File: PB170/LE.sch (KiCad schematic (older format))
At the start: 7 parts

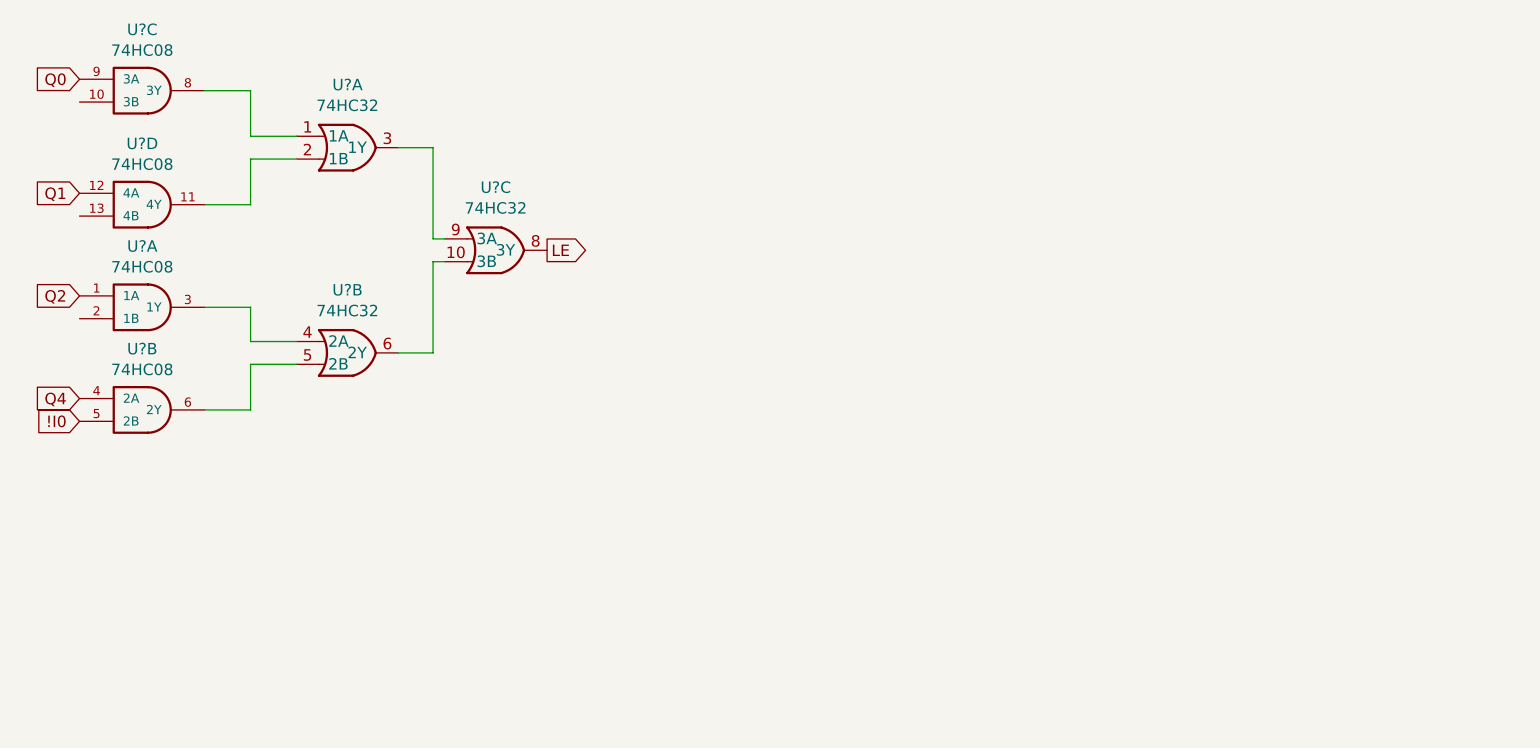
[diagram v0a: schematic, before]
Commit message: added some labels
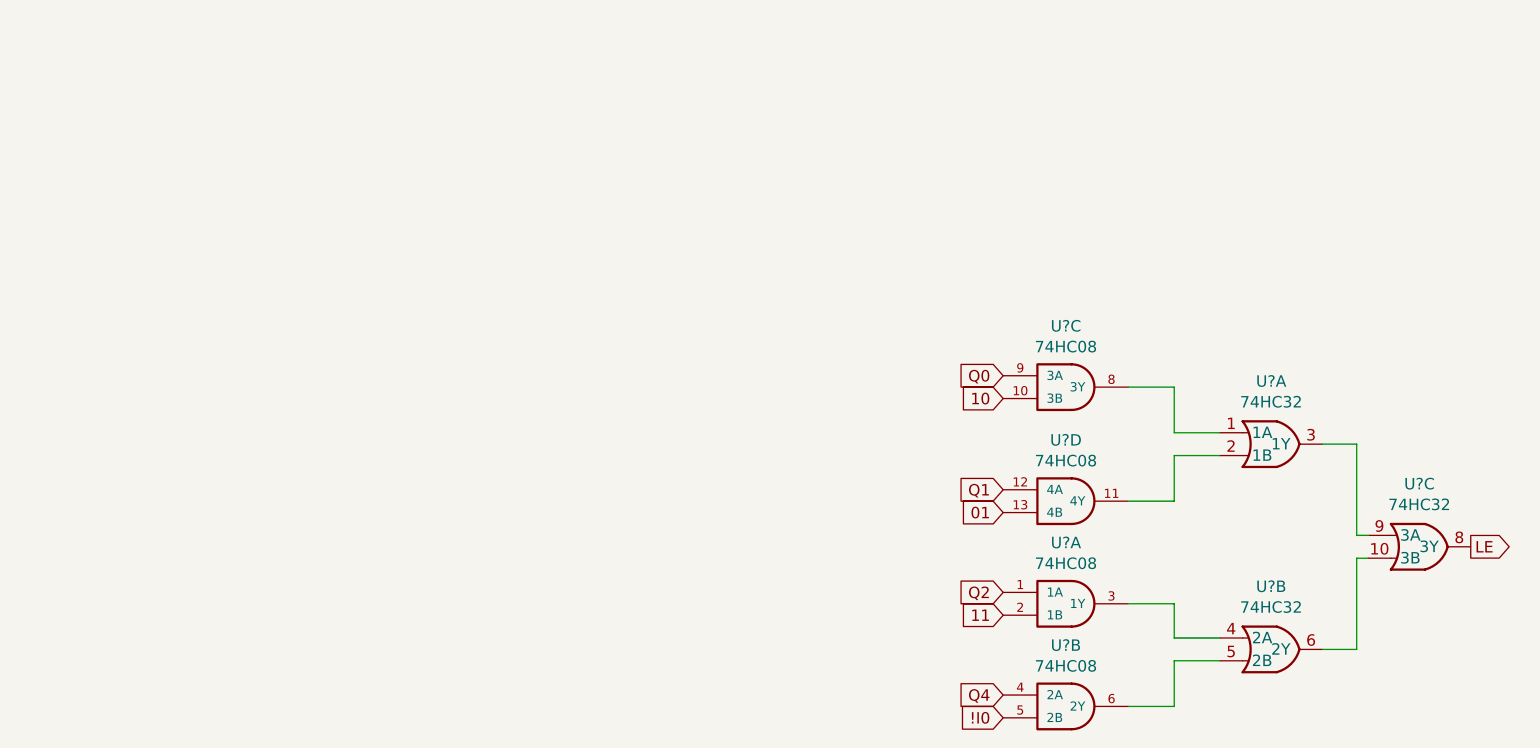
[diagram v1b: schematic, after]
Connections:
- net 10: now reaches U?.10 (3B)
- net 01: now reaches U?.13 (4B)
- net 11: now reaches U?.2 (1B)
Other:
- moved on the sheet: U?A, U?B, U?C, U?D
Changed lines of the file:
@@
 $Descr A4 11693 8268
 encoding utf-8
-Sheet 6 7
+Sheet 6 6
 Title ""
 Date ""
@@
 L PB170:74HC08 U?
 U 3 1 602725DE
-P 1550 1550
-F 0 "U?" H 1575 1817 50  0000 C CNN
-F 1 "74HC08" H 1575 1726 50  0000 C CNN
-F 2 "Housings_SOIC:SOIC-14_3.9x8.7mm_Pitch1.27mm" H 1550 1550 50  0001 C CNN
-F 3 "https://datasheet.lcsc.com/szlcsc/Nexperia-74HC08D-653_C5593.pdf" H 1550 1550 50  0001 C CNN
-F 4 "C5593" H 1550 1550 50  0001 C CNN "LCSC"
-	3    1550 1550
+P 5600 2850
+F 0 "U?" H 5625 3117 50  0000 C CNN
+F 1 "74HC08" H 5625 3026 50  0000 C CNN
+F 2 "Housings_SOIC:SOIC-14_3.9x8.7mm_Pitch1.27mm" H 5600 2850 50  0001 C CNN
+F 3 "https://datasheet.lcsc.com/szlcsc/Nexperia-74HC08D-653_C5593.pdf" H 5600 2850 50  0001 C CNN
+F 4 "C5593" H 5600 2850 50  0001 C CNN "LCSC"
+	3    5600 2850
 	1    0    0    -1
 $EndComp
@@
 L PB170:74HC08 U?
 U 4 1 602728F1
-P 1550 2050
-F 0 "U?" H 1575 2317 50  0000 C CNN
-F 1 "74HC08" H 1575 2226 50  0000 C CNN
-F 2 "Housings_SOIC:SOIC-14_3.9x8.7mm_Pitch1.27mm" H 1550 2050 50  0001 C CNN
-F 3 "https://datasheet.lcsc.com/szlcsc/Nexperia-74HC08D-653_C5593.pdf" H 1550 2050 50  0001 C CNN
-F 4 "C5593" H 1550 2050 50  0001 C CNN "LCSC"
-	4    1550 2050
+P 5600 3350
+F 0 "U?" H 5625 3617 50  0000 C CNN
+F 1 "74HC08" H 5625 3526 50  0000 C CNN
+F 2 "Housings_SOIC:SOIC-14_3.9x8.7mm_Pitch1.27mm" H 5600 3350 50  0001 C CNN
+F 3 "https://datasheet.lcsc.com/szlcsc/Nexperia-74HC08D-653_C5593.pdf" H 5600 3350 50  0001 C CNN
+F 4 "C5593" H 5600 3350 50  0001 C CNN "LCSC"
+	4    5600 3350
 	1    0    0    -1
 $EndComp
@@
 L PB170:74HC08 U?
 U 1 1 60272E03
-P 1550 2500
-F 0 "U?" H 1575 2767 50  0000 C CNN
-F 1 "74HC08" H 1575 2676 50  0000 C CNN
-F 2 "Housings_SOIC:SOIC-14_3.9x8.7mm_Pitch1.27mm" H 1550 2500 50  0001 C CNN
-F 3 "https://datasheet.lcsc.com/szlcsc/Nexperia-74HC08D-653_C5593.pdf" H 1550 2500 50  0001 C CNN
-F 4 "C5593" H 1550 2500 50  0001 C CNN "LCSC"
-	1    1550 2500
+P 5600 3800
+F 0 "U?" H 5625 4067 50  0000 C CNN
+F 1 "74HC08" H 5625 3976 50  0000 C CNN
+F 2 "Housings_SOIC:SOIC-14_3.9x8.7mm_Pitch1.27mm" H 5600 3800 50  0001 C CNN
+F 3 "https://datasheet.lcsc.com/szlcsc/Nexperia-74HC08D-653_C5593.pdf" H 5600 3800 50  0001 C CNN
+F 4 "C5593" H 5600 3800 50  0001 C CNN "LCSC"
+	1    5600 3800
 	1    0    0    -1
 $EndComp
@@
 L PB170:74HC08 U?
 U 2 1 602733B4
-P 1550 2950
-F 0 "U?" H 1575 3217 50  0000 C CNN
-F 1 "74HC08" H 1575 3126 50  0000 C CNN
-F 2 "Housings_SOIC:SOIC-14_3.9x8.7mm_Pitch1.27mm" H 1550 2950 50  0001 C CNN
-F 3 "https://datasheet.lcsc.com/szlcsc/Nexperia-74HC08D-653_C5593.pdf" H 1550 2950 50  0001 C CNN
-F 4 "C5593" H 1550 2950 50  0001 C CNN "LCSC"
-	2    1550 2950
+P 5600 4250
+F 0 "U?" H 5625 4517 50  0000 C CNN
+F 1 "74HC08" H 5625 4426 50  0000 C CNN
+F 2 "Housings_SOIC:SOIC-14_3.9x8.7mm_Pitch1.27mm" H 5600 4250 50  0001 C CNN
+F 3 "https://datasheet.lcsc.com/szlcsc/Nexperia-74HC08D-653_C5593.pdf" H 5600 4250 50  0001 C CNN
+F 4 "C5593" H 5600 4250 50  0001 C CNN "LCSC"
+	2    5600 4250
 	1    0    0    -1
 $EndComp
@@
 L PB170:74HC32 U?
 U 1 1 60274388
-P 2500 1800
-F 0 "U?" H 2475 2075 50  0000 C CNN
-F 1 "74HC32" H 2475 1984 50  0000 C CNN
-F 2 "Housings_SOIC:SOIC-14_3.9x8.7mm_Pitch1.27mm" H 1950 2000 50  0001 C CNN
-F 3 "https://datasheet.lcsc.com/szlcsc/Nexperia-74HC32D-653_C5632.pdf" H 1950 2000 50  0001 C CNN
-F 4 "C5632" H 2500 1800 50  0001 C CNN "LCSC"
-	1    2500 1800
+P 6550 3100
+F 0 "U?" H 6525 3375 50  0000 C CNN
+F 1 "74HC32" H 6525 3284 50  0000 C CNN
+F 2 "Housings_SOIC:SOIC-14_3.9x8.7mm_Pitch1.27mm" H 6000 3300 50  0001 C CNN
+F 3 "https://datasheet.lcsc.com/szlcsc/Nexperia-74HC32D-653_C5632.pdf" H 6000 3300 50  0001 C CNN
+F 4 "C5632" H 6550 3100 50  0001 C CNN "LCSC"
+	1    6550 3100
 	1    0    0    -1
 $EndComp
@@
 L PB170:74HC32 U?
 U 2 1 60274C1B
-P 2500 2700
-F 0 "U?" H 2475 2975 50  0000 C CNN
-F 1 "74HC32" H 2475 2884 50  0000 C CNN
-F 2 "Housings_SOIC:SOIC-14_3.9x8.7mm_Pitch1.27mm" H 1950 2900 50  0001 C CNN
-F 3 "https://datasheet.lcsc.com/szlcsc/Nexperia-74HC32D-653_C5632.pdf" H 1950 2900 50  0001 C CNN
-F 4 "C5632" H 2500 2700 50  0001 C CNN "LCSC"
-	2    2500 2700
+P 6550 4000
+F 0 "U?" H 6525 4275 50  0000 C CNN
+F 1 "74HC32" H 6525 4184 50  0000 C CNN
+F 2 "Housings_SOIC:SOIC-14_3.9x8.7mm_Pitch1.27mm" H 6000 4200 50  0001 C CNN
+F 3 "https://datasheet.lcsc.com/szlcsc/Nexperia-74HC32D-653_C5632.pdf" H 6000 4200 50  0001 C CNN
+F 4 "C5632" H 6550 4000 50  0001 C CNN "LCSC"
+	2    6550 4000
 	1    0    0    -1
 $EndComp
@@
 L PB170:74HC32 U?
 U 3 1 602758C2
-P 3150 2250
-F 0 "U?" H 3125 2525 50  0000 C CNN
-F 1 "74HC32" H 3125 2434 50  0000 C CNN
-F 2 "Housings_SOIC:SOIC-14_3.9x8.7mm_Pitch1.27mm" H 2600 2450 50  0001 C CNN
-F 3 "https://datasheet.lcsc.com/szlcsc/Nexperia-74HC32D-653_C5632.pdf" H 2600 2450 50  0001 C CNN
-F 4 "C5632" H 3150 2250 50  0001 C CNN "LCSC"
-	3    3150 2250
+P 7200 3550
+F 0 "U?" H 7175 3825 50  0000 C CNN
+F 1 "74HC32" H 7175 3734 50  0000 C CNN
+F 2 "Housings_SOIC:SOIC-14_3.9x8.7mm_Pitch1.27mm" H 6650 3750 50  0001 C CNN
+F 3 "https://datasheet.lcsc.com/szlcsc/Nexperia-74HC32D-653_C5632.pdf" H 6650 3750 50  0001 C CNN
+F 4 "C5632" H 7200 3550 50  0001 C CNN "LCSC"
+	3    7200 3550
 	1    0    0    -1
 $EndComp
 Wire Wire Line
-	1850 1550 2050 1550
+	5900 2850 6100 2850
 Wire Wire Line
-	2050 1550 2050 1750
+	6100 2850 6100 3050
 Wire Wire Line
-	2050 1750 2250 1750
+	6100 3050 6300 3050
 Wire Wire Line
-	1850 2050 2050 2050
+	5900 3350 6100 3350
 Wire Wire Line
-	2050 2050 2050 1850
+	6100 3350 6100 3150
 Wire Wire Line
-	2050 1850 2250 1850
+	6100 3150 6300 3150
 Wire Wire Line
-	1850 2500 2050 2500
+	5900 3800 6100 3800
 Wire Wire Line
-	2050 2500 2050 2650
+	6100 3800 6100 3950
 Wire Wire Line
-	2050 2650 2250 2650
+	6100 3950 6300 3950
 Wire Wire Line
-	1850 2950 2050 2950
+	5900 4250 6100 4250
 Wire Wire Line
-	2050 2950 2050 2750
+	6100 4250 6100 4050
 Wire Wire Line
-	2050 2750 2250 2750
+	6100 4050 6300 4050
 Wire Wire Line
-	2700 1800 2850 1800
+	6750 3100 6900 3100
 Wire Wire Line
-	2850 1800 2850 2200
+	6900 3100 6900 3500
 Wire Wire Line
-	2850 2200 2900 2200
+	6900 3500 6950 3500
 Wire Wire Line
-	2700 2700 2850 2700
+	6750 4000 6900 4000
 Wire Wire Line
-	2850 2700 2850 2300
+	6900 4000 6900 3600
 Wire Wire Line
-	2850 2300 2900 2300
-Text GLabel 3350 2250 2    50   Output ~ 0
+	6900 3600 6950 3600
+Text GLabel 7400 3550 2    50   Output ~ 0
 LE
-Text GLabel 1300 1500 0    50   Input ~ 0
+Text GLabel 5350 2800 0    50   Input ~ 0
 Q0
-Text GLabel 1300 2000 0    50   Input ~ 0
+Text GLabel 5350 3300 0    50   Input ~ 0
 Q1
-Text GLabel 1300 2450 0    50   Input ~ 0
+Text GLabel 5350 3750 0    50   Input ~ 0
 Q2
-Text GLabel 1300 2900 0    50   Input ~ 0
+Text GLabel 5350 4200 0    50   Input ~ 0
 Q4
-Text GLabel 1300 3000 0    50   Input ~ 0
+Text GLabel 5350 4300 0    50   Input ~ 0
 !I0
+Text GLabel 5350 2900 0    50   Input ~ 0
+10
+Text GLabel 5350 3400 0    50   Input ~ 0
+01
+Text GLabel 5350 3850 0    50   Input ~ 0
+11
 $EndSCHEMATC
